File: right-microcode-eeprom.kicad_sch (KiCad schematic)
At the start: 20 parts, among them U37 AT28C64B, U53 74HCT04

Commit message: add pdf for instructions
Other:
- company: (none) -> TBR Designs
- title: (none) -> 8-bit CPU
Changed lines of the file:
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@@
 (kicad_sch (version 20230121) (generator eeschema)
   (paper "A4")
+  (title_block
+    (title "8-bit CPU")
+    (date "2023-11-28")
+    (rev "1.0")
+    (company "TBR Designs")
+  )
   (junction (at 118.11 55.88) (diameter 0) (color 0 0 0 0)
   )

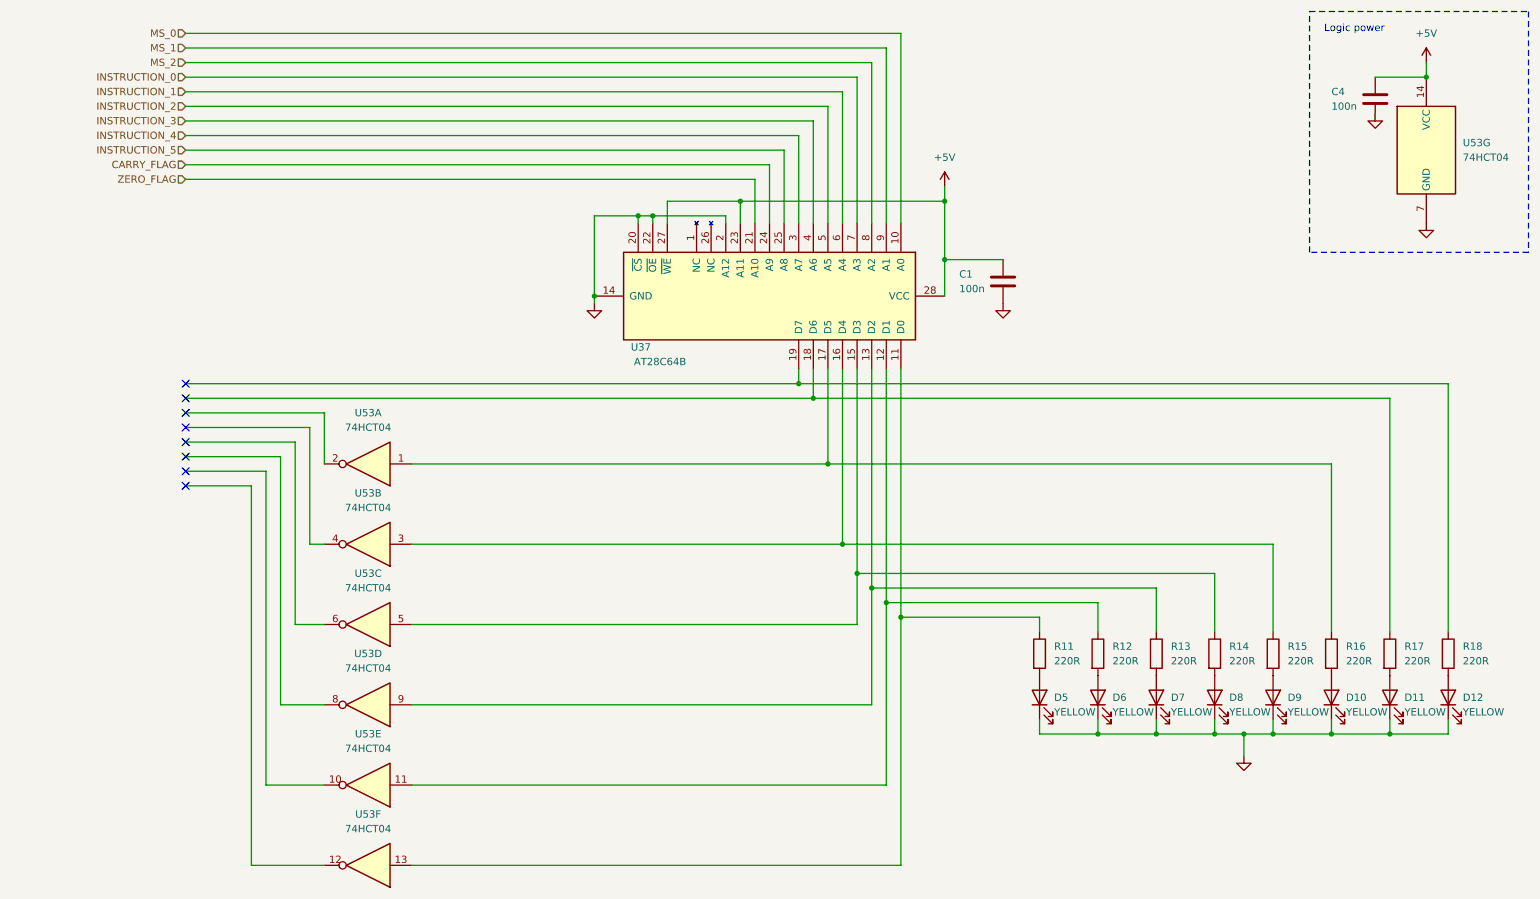
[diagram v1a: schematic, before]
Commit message: added stack and x register.  Added logic for stack_address so ram address 7 gets passes and ram address 8 is high
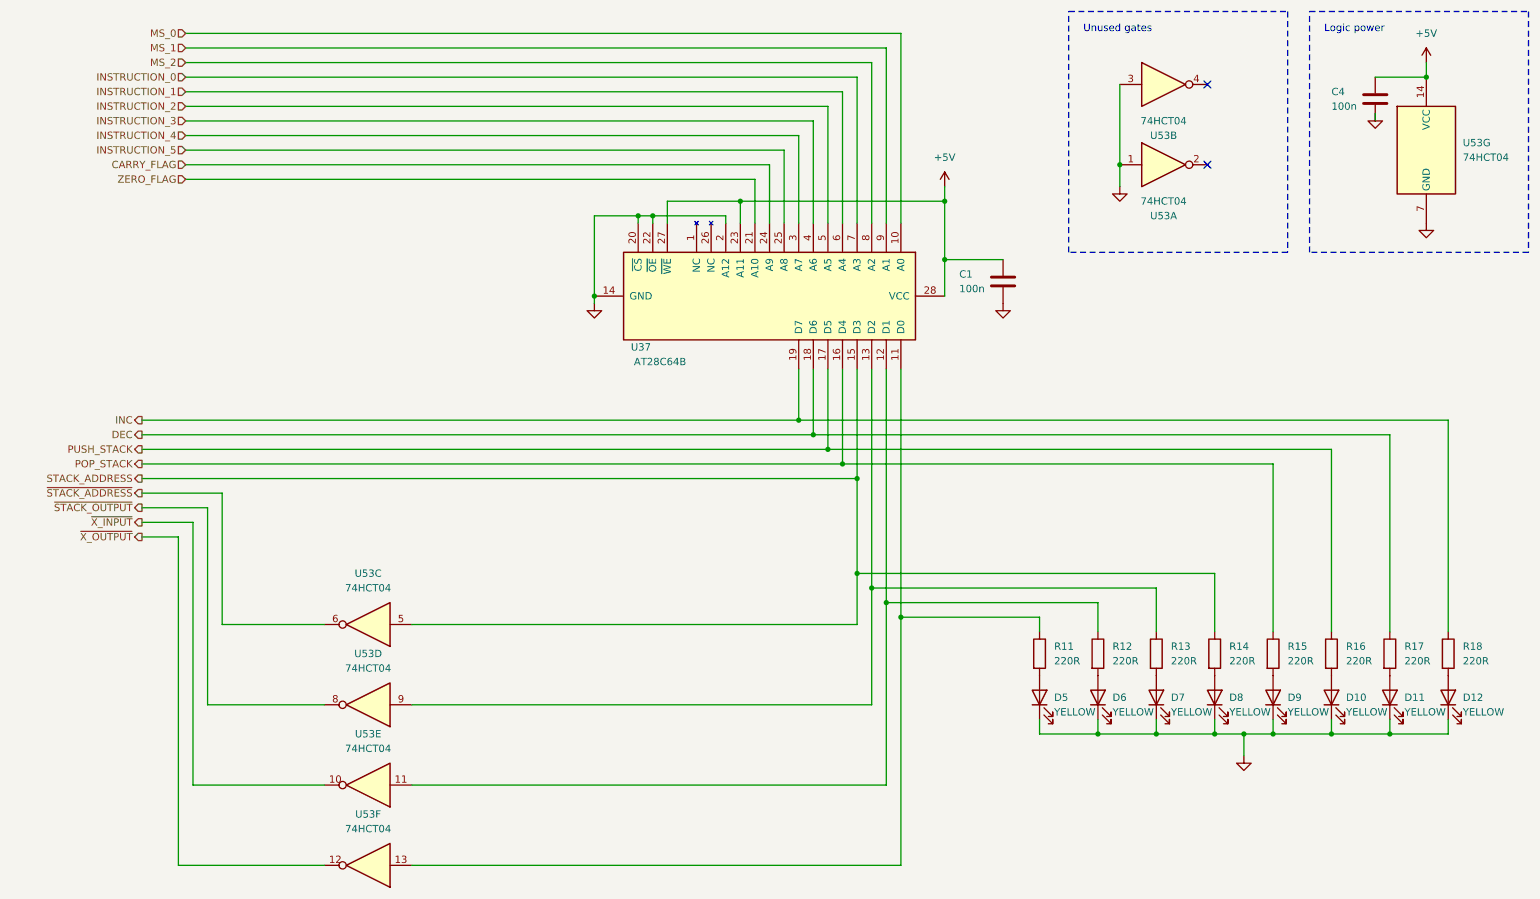
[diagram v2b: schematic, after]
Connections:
- net GND: now also U53.1, U53.3
- net ~{X_OUTPUT}: now reaches U53.12
- net STACK_ADDRESS: now reaches R14.1, U37.15 (D3), U53.5
- net POP_STACK: now reaches R15.1, U37.16 (D4)
- net POP_STACK: no longer U53.3
- net PUSH_STACK: now reaches R16.1, U37.17 (D5)
- net PUSH_STACK: no longer U53.1
- net DEC: now reaches R17.1, U37.18 (D6)
- net INC: now reaches R18.1, U37.19 (D7)
- net ~{STACK_ADDRESS}: now reaches U53.6
- net ~{STACK_OUTPUT}: now reaches U53.8
- net ~{X_INPUT}: now reaches U53.10
- no-connect marks 8 -> 2
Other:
- note added: "Unused gates"

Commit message: add arduino headers for programming
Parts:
- U53: footprint (none) -> Package_DIP:DIP-14_W7.62mm
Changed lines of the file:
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@@
       (effects (font (size 1.27 1.27)))
     )
-    (property "Footprint" "" (at 71.12 168.91 0)
+    (property "Footprint" "Package_DIP:DIP-14_W7.62mm" (at 71.12 168.91 0)
       (effects (font (size 1.27 1.27)) hide)
     )
@@
       (effects (font (size 1.27 1.27)))
     )
-    (property "Footprint" "" (at 209.55 46.99 0)
+    (property "Footprint" "Package_DIP:DIP-14_W7.62mm" (at 209.55 46.99 0)
       (effects (font (size 1.27 1.27)) hide)
     )
@@
       (effects (font (size 1.27 1.27)) (justify left))
     )
-    (property "Footprint" "" (at 255.27 44.45 0)
+    (property "Footprint" "Package_DIP:DIP-14_W7.62mm" (at 255.27 44.45 0)
       (effects (font (size 1.27 1.27)) hide)
     )
@@
       (effects (font (size 1.27 1.27)))
     )
-    (property "Footprint" "" (at 71.12 127 0)
+    (property "Footprint" "Package_DIP:DIP-14_W7.62mm" (at 71.12 127 0)
       (effects (font (size 1.27 1.27)) hide)
     )
@@
       (effects (font (size 1.27 1.27)))
     )
-    (property "Footprint" "" (at 71.12 140.97 0)
+    (property "Footprint" "Package_DIP:DIP-14_W7.62mm" (at 71.12 140.97 0)
       (effects (font (size 1.27 1.27)) hide)
     )
@@
       (effects (font (size 1.27 1.27)))
     )
-    (property "Footprint" "" (at 71.12 154.94 0)
+    (property "Footprint" "Package_DIP:DIP-14_W7.62mm" (at 71.12 154.94 0)
       (effects (font (size 1.27 1.27)) hide)
     )
@@
       (effects (font (size 1.27 1.27)))
     )
-    (property "Footprint" "" (at 209.55 33.02 0)
-      (effects (font (size 1.27 1.27)) hide)
-    )
+    (property "Footprint" "Package_DIP:DIP-14_W7.62mm" (at 209.55 33.02 0)
+      (effects (font (size 1.27 1.27)) hide)
+    )

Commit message: cleanup
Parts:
- D10, D11, D12, D5, D6, D7, D8, D9: value YELLOW -> BLUE
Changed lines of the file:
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@@
         )
         (path "/100bb8d1-c3d6-4e1f-87b6-72e4e187243c/cbe1ebf3-0fd2-468b-b752-73c1c63eb76e/b366b11d-2830-45f0-9c94-a2792c6fd84a"
-          (reference "#PWR0200") (unit 1)
+          (reference "#PWR0203") (unit 1)
         )
       )
@@
         )
         (path "/100bb8d1-c3d6-4e1f-87b6-72e4e187243c/cbe1ebf3-0fd2-468b-b752-73c1c63eb76e/b366b11d-2830-45f0-9c94-a2792c6fd84a"
-          (reference "#PWR0202") (unit 1)
+          (reference "#PWR0205") (unit 1)
         )
       )
@@
       (effects (font (size 1.27 1.27)) (justify right))
     )
-    (property "Value" "YELLOW" (at 261.62 142.24 90)
+    (property "Value" "BLUE" (at 261.62 142.24 90)
       (effects (font (size 1.27 1.27)) (justify right))
     )
@@
       (effects (font (size 1.27 1.27)) (justify right))
     )
-    (property "Value" "YELLOW" (at 251.46 142.24 90)
+    (property "Value" "BLUE" (at 251.46 142.24 90)
       (effects (font (size 1.27 1.27)) (justify right))
     )
@@
       (effects (font (size 1.27 1.27)) (justify right))
     )
-    (property "Value" "YELLOW" (at 210.82 142.24 90)
+    (property "Value" "BLUE" (at 210.82 142.24 90)
       (effects (font (size 1.27 1.27)) (justify right))
     )
@@
         )
         (path "/100bb8d1-c3d6-4e1f-87b6-72e4e187243c/cbe1ebf3-0fd2-468b-b752-73c1c63eb76e/b366b11d-2830-45f0-9c94-a2792c6fd84a"
-          (reference "#PWR0203") (unit 1)
+          (reference "#PWR0206") (unit 1)
         )
       )
@@
         )
         (path "/100bb8d1-c3d6-4e1f-87b6-72e4e187243c/cbe1ebf3-0fd2-468b-b752-73c1c63eb76e/b366b11d-2830-45f0-9c94-a2792c6fd84a"
-          (reference "#PWR0198") (unit 1)
+          (reference "#PWR0201") (unit 1)
         )
       )
@@
         )
         (path "/100bb8d1-c3d6-4e1f-87b6-72e4e187243c/cbe1ebf3-0fd2-468b-b752-73c1c63eb76e/b366b11d-2830-45f0-9c94-a2792c6fd84a"
-          (reference "#PWR0201") (unit 1)
+          (reference "#PWR0204") (unit 1)
         )
       )
@@
       (effects (font (size 1.27 1.27)) (justify right))
     )
-    (property "Value" "YELLOW" (at 231.14 142.24 90)
+    (property "Value" "BLUE" (at 231.14 142.24 90)
       (effects (font (size 1.27 1.27)) (justify right))
     )
@@
       (effects (font (size 1.27 1.27)) (justify right))
     )
-    (property "Value" "YELLOW" (at 190.5 142.24 90)
+    (property "Value" "BLUE" (at 190.5 142.24 90)
       (effects (font (size 1.27 1.27)) (justify right))
     )
@@
         )
         (path "/100bb8d1-c3d6-4e1f-87b6-72e4e187243c/cbe1ebf3-0fd2-468b-b752-73c1c63eb76e/b366b11d-2830-45f0-9c94-a2792c6fd84a"
-          (reference "#PWR0197") (unit 1)
+          (reference "#PWR0200") (unit 1)
         )
       )
@@
       (effects (font (size 1.27 1.27)) (justify right))
     )
-    (property "Value" "YELLOW" (at 220.98 142.24 90)
+    (property "Value" "BLUE" (at 220.98 142.24 90)
       (effects (font (size 1.27 1.27)) (justify right))
     )
@@
       (effects (font (size 1.27 1.27)) (justify right))
     )
-    (property "Value" "YELLOW" (at 241.3 142.24 90)
+    (property "Value" "BLUE" (at 241.3 142.24 90)
       (effects (font (size 1.27 1.27)) (justify right))
     )
@@
         )
         (path "/100bb8d1-c3d6-4e1f-87b6-72e4e187243c/cbe1ebf3-0fd2-468b-b752-73c1c63eb76e/b366b11d-2830-45f0-9c94-a2792c6fd84a"
-          (reference "#PWR0199") (unit 1)
+          (reference "#PWR0202") (unit 1)
         )
       )
@@
         )
         (path "/100bb8d1-c3d6-4e1f-87b6-72e4e187243c/cbe1ebf3-0fd2-468b-b752-73c1c63eb76e/b366b11d-2830-45f0-9c94-a2792c6fd84a"
-          (reference "#PWR0196") (unit 1)
+          (reference "#PWR0199") (unit 1)
         )
       )
@@
       (effects (font (size 1.27 1.27)) (justify right))
     )
-    (property "Value" "YELLOW" (at 200.66 142.24 90)
-      (effects (font (size 1.27 1.27)) (justify right))
-    )
+    (property "Value" "BLUE" (at 200.66 142.24 90)
+      (effects (font (size 1.27 1.27)) (justify right))
+    )

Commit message: trying to solve issues
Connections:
- net GND: now also U53.11
- net X_INPUT: now reaches R12.1, U37.12 (D1)
- net X_INPUT: no longer U53.11
- net CARRY_FLAG renamed EEPROM_9
- net INSTRUCTION_0 renamed EEPROM_3
- net INSTRUCTION_1 renamed EEPROM_4
- net INSTRUCTION_2 renamed EEPROM_5
- net INSTRUCTION_3 renamed EEPROM_6
- net INSTRUCTION_4 renamed EEPROM_7
- net INSTRUCTION_5 renamed EEPROM_8
- net ZERO_FLAG renamed EEPROM_10
- net ~{X_INPUT}: no longer names the net of U53.10
- no-connect marks 2 -> 3
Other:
- moved on the sheet: U53E
